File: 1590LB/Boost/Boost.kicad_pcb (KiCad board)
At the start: 2 copper layers, 45 x 45 mm, 44 parts, among them J101 Barrel_Jack_Switch, J102 AudioJack2_SwitchT, J103 AudioJack2_SwitchT, Q101 PMV250, Q201 MMBF5103, Q202 BC847C, Q203 BC857C, Q204 NMB2227A, Q205 DMMT5401, Q206 DMMT5551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

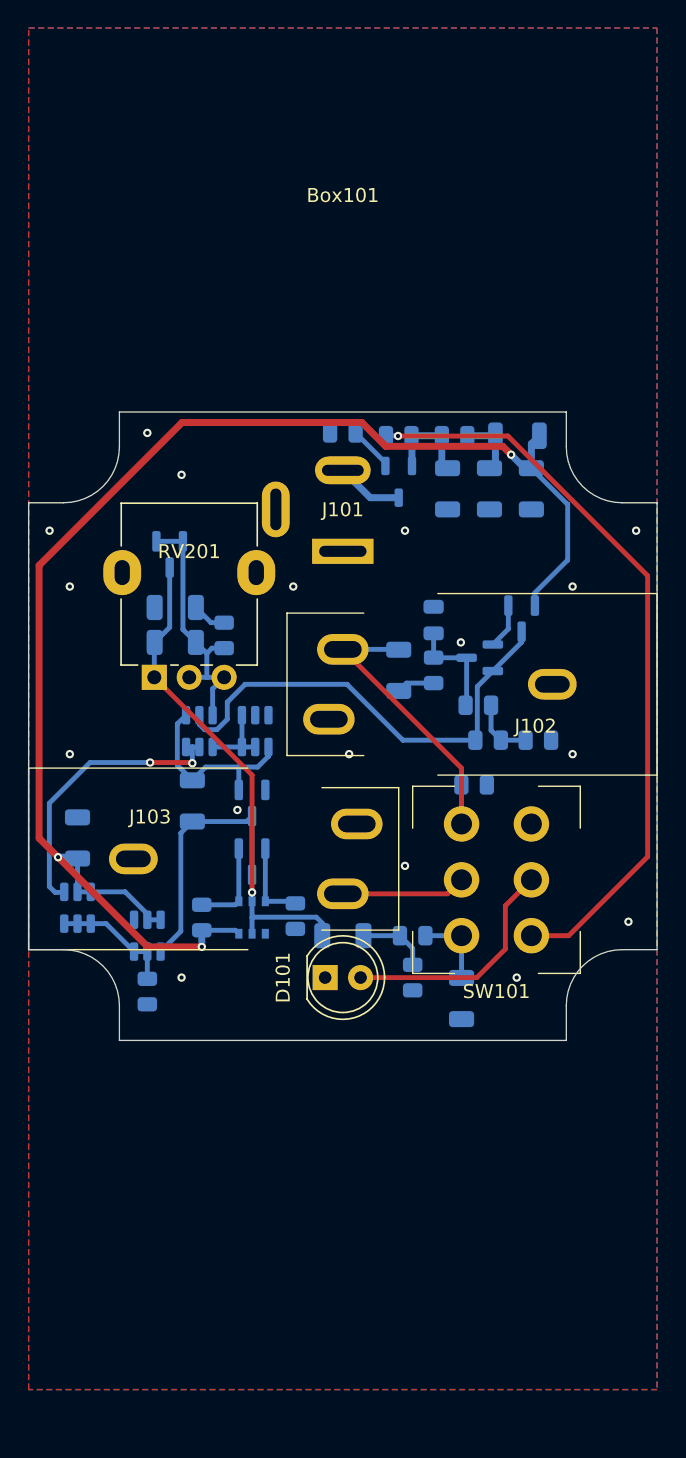
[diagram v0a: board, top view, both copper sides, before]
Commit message: Alternate boost circuit layout
I'm not sure this fits vertically in a 1590LB, but the "everything on
top" model means that the audio jacks are very high up.  Which is not
great from a hole drilling standpoint.

So try putting the audio and DC power jacks on the back of the board,
moving the surface-mount components to the front.

And to make things fit - and because I feel like having done an op-amp
using discrete components - go back to just using an actual op-amp now.

Signed-off-by: Linus Torvalds <torvalds@linux-foundation.org>
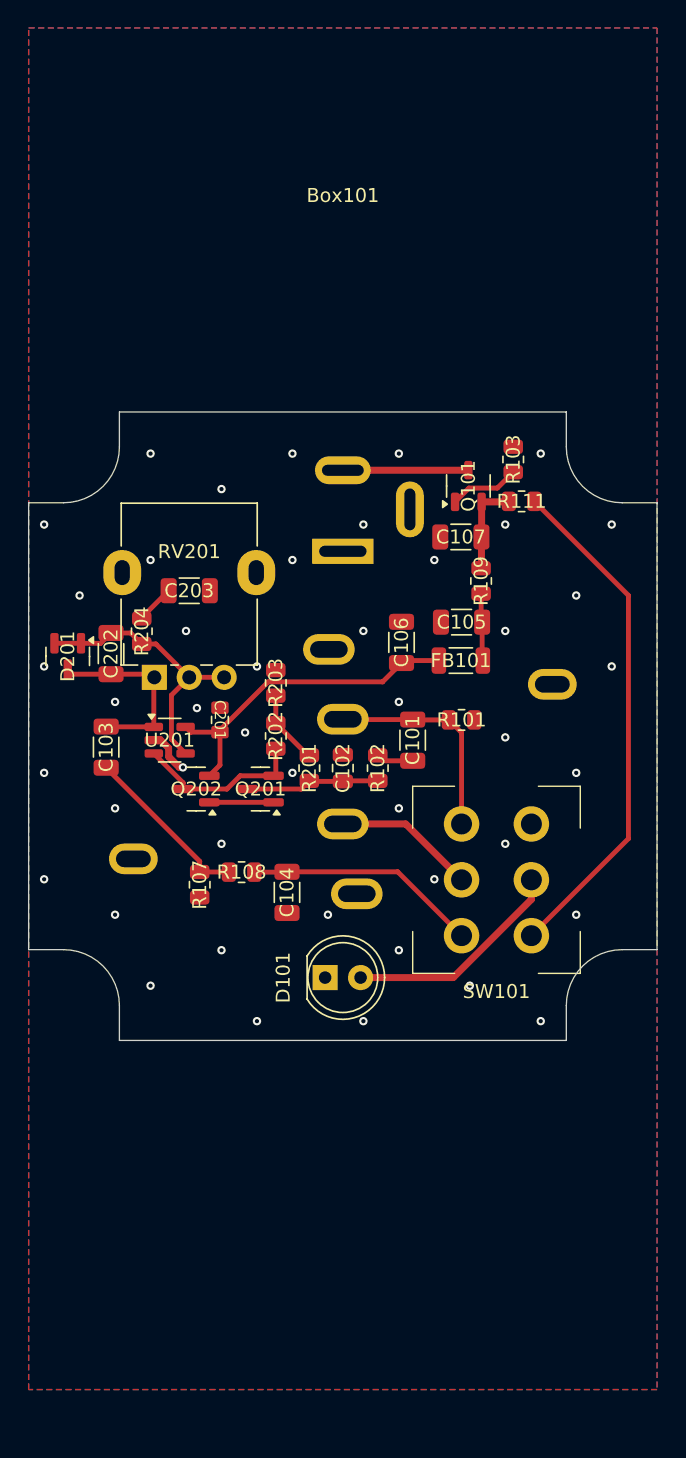
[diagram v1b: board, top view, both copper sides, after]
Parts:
- removed C204: 10uF, Capacitor_SMD:C_1206_3216Metric
- removed the D201 at (93.5, 109.7)
- removed the Q202 at (93.5, 105.5)
- removed Q204: NMB2227A, Package_SO:TSOP-6_1.65x3.05mm_P0.95mm
- removed Q205, Q207, Q208: DMMT5401, Package_TO_SOT_SMD:SOT-23-6
- removed Q206: DMMT5551, Package_TO_SOT_SMD:SOT-23-6
- removed the R204 at (89.9, 113.7)
- removed R205: 47k, Resistor_SMD:R_0805_2012Metric
- removed R207: 5k6, Resistor_SMD:R_0805_2012Metric
- added U201: OPA1655DBV, Package_TO_SOT_SMD:SOT-23-5, F.Cu at (87.6, 101.0)
- C101, C102, C103, C104, C105, C106, C107, C202, C203, FB101, Q101, Q201, R101, R102, R103, R107, R108, R109, R111, R201, R202, R203: moved to F.Cu
- C201: value 1nF -> 0.1uF; footprint Capacitor_SMD:C_1206_3216Metric -> Mylib:C_0704_1810Metric; moved to F.Cu
- D201: renamed from D202; moved to F.Cu
- J101, J102, J103: moved to B.Cu
- Q202: renamed from Q203; moved to F.Cu
- R204: renamed from R206; moved to F.Cu
- moved Q202 26.3 mm to (89.5, 104.5), turned to 180 degrees
- moved C103 21.7 mm to (83.0, 101.5), turned to -90 degrees
- moved R203 19.2 mm to (95.2, 96.9), turned to 90 degrees
- moved Q201 18.3 mm to (94.1, 104.5)
- moved R107 16.6 mm to (89.8, 111.3)
- moved FB101 16.6 mm to (108.5, 95.3), turned to 0 degrees
- moved R202 15.2 mm to (95.2, 100.7), turned to 90 degrees
- moved C104 14.6 mm to (96.0, 111.9)
- moved C106 14.4 mm to (104.2, 94.0), turned to -90 degrees
- moved R108 13.1 mm to (92.8, 110.5)
- moved R201 12.9 mm to (97.6, 103.0), turned to 90 degrees
- moved C102 12.4 mm to (100.0, 103.0)
- moved R103 12.3 mm to (112.2, 80.9), turned to 90 degrees
- moved R109 10.6 mm to (109.9, 89.6), turned to -90 degrees
- moved D201 10.3 mm to (80.3, 95.0)
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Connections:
- C201 pad 1: SRC2 -> GND
- C201 pad 2: LTP_OUT -> +VA
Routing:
- net +VA: track 104.5 -> 23.9 mm, vias 3 -> 0
- net OUTPUT: track 35.7 -> 13.4 mm, vias 1 -> 0
- net BUFFERED: track 33.4 -> 12.3 mm
- net SRC1: track 20.8 -> 0.00 mm, vias 2 -> 0
- net SRC2: track 18.9 -> 0.00 mm
- net Net-(SW101A-C): track 53.7 -> 36.8 mm, vias 1 -> 0
- net LTP_OUT: track 13.9 -> 0.00 mm
- net OUT^{STOMP}: track 5.61 -> 16.7 mm
- net SRC_BASE: track 8.73 -> 0.00 mm
- net Net-(C103-Pad2): track 5.08 -> 12.3 mm
- net Net-(D201-A): track 6.88 -> 0.00 mm
- net Net-(D201-K): track 5.99 -> 0.00 mm
- net IN^{CONN}: track 22.4 -> 16.4 mm
- net Net-(Q205B-C): track 5.32 -> 0.00 mm
- net PWRIN: track 4.81 -> 8.99 mm
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
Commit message: Make the boost circuit a bit more interesting
The clean boost with some clipping was very boring, both from a sound
and a circuit standpoint.

This one isn't any better from a sound standpoint, but at least it's a
bit more interesting.  Instead of a boost pot and clipping diodes, this
has a pot that affects the biasing of the input JFET, and a fixed 10x
voltage boost with a final volume pot.

End result: it also clips, but the clipping is based on how badly the
input transistor is biased, so now you have a bit more control over the
result.

Useful? No.  But I'm back to using discrete components, because the
whole op-amp thing was just too boring.  If I want to use pre-made
circuits, I can do that on the MCU board, let's keep the analog boards
discrete.

That said, I've made the resistors and capacitors small, because I'll
just use this one for the JLCPCB assembly testing.  I did send off a
copy of the MCU board too, which is probably completely stupid - the
first PCBA board I do shouldn't have been that complex.  But maybe it
works (after I figure out the programming - even if the board is fine,
I'll have to do the SW side too to even test it).

Anyway, this one I can have assembled - and test - without then having
to write any code for various i2s things that I have no idea about.

Oh, and I still call this a "1590LB" boost board, even though I actually
ended up deciding that I'll just 3D-print the enclosure.  So it's not
really a 1590LB, it's a 45x50mm board that I'll just print a custom
enclosure for.  I actually really liked how one of my test enclosures
ended up looking, and not being limited to standard aluminum boxes is
liberating.

Signed-off-by: Linus Torvalds <torvalds@linux-foundation.org>
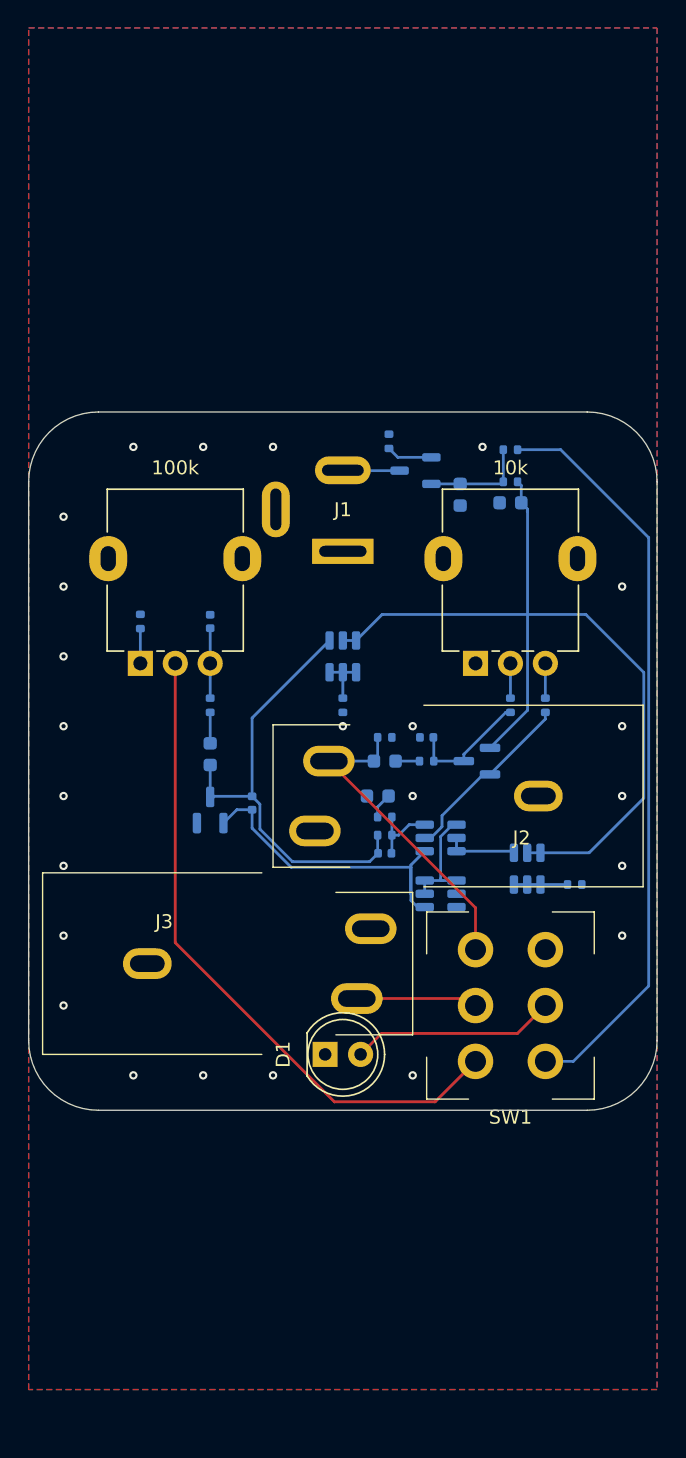
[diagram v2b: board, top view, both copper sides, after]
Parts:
- removed Box101: 1590LB, Mylib:1590LB
- removed C105: 10uF, Capacitor_SMD:C_1206_3216Metric
- removed C106: 1uF, Capacitor_SMD:C_1206_3216Metric
- removed C201: 0.1uF, Mylib:C_0704_1810Metric
- removed D201: MMBD1203, Package_TO_SOT_SMD:SOT-23
- removed FB101: FerriteBead, Inductor_SMD:L_1206_3216Metric
- removed Q201: MMBF5103, Package_TO_SOT_SMD:SOT-23
- removed Q202: BC857C, Package_TO_SOT_SMD:SOT-23
- removed R107: 1MEG, Resistor_SMD:R_0805_2012Metric
- removed R109: 100R, Resistor_SMD:R_0805_2012Metric
- removed R202: 2k2, Resistor_SMD:R_0805_2012Metric
- removed RV201: 100k, Mylib:Potentiometer_9mm_MP
- removed U201: OPA1655DBV, Package_TO_SOT_SMD:SOT-23-5
- added C4: 10uF, Capacitor_SMD:C_0603_1608Metric, B.Cu at (112.0, 84.0)
- added C7: 1nF, Capacitor_SMD:C_0402_1005Metric, B.Cu at (93.5, 105.5)
- added Q2: MMBFJ309L, Package_TO_SOT_SMD:SOT-23, B.Cu at (109.6, 102.5)
- added Q3: BC847C, Package_TO_SOT_SMD:SOT-23, B.Cu at (90.5, 106.0)
- added Q4: DMMT5401, Package_TO_SOT_SMD:SOT-23-6, B.Cu at (107.0, 108.0)
- added Q5: DMMT5551, Package_TO_SOT_SMD:SOT-23-6, B.Cu at (107.0, 112.0)
- added Q6: DMMT5401, Package_TO_SOT_SMD:SOT-23-6, B.Cu at (113.2, 110.2)
- added Q7: DMMT5401, Package_TO_SOT_SMD:SOT-23-6, B.Cu at (100.0, 95.0)
- added R10: 100k, Resistor_SMD:R_0402_1005Metric, B.Cu at (103.0, 107.8)
- added R12: 5k6, Resistor_SMD:R_0402_1005Metric, B.Cu at (116.6, 111.3)
- added R13: 5k6, Resistor_SMD:R_0402_1005Metric, B.Cu at (100.0, 98.5)
- added R5: 33R, Resistor_SMD:R_0402_1005Metric, B.Cu at (112.0, 82.5)
- added R7: 10k, Resistor_SMD:R_0402_1005Metric, B.Cu at (85.5, 92.5)
- added RV1: 100k, Mylib:Potentiometer_9mm_MP, F.Cu at (88.0, 88.0)
- added RV2: 10k, Mylib:Potentiometer_9mm_MP, F.Cu at (112.0, 88.0)
- C1: renamed from C101; footprint Capacitor_SMD:C_1206_3216Metric -> Capacitor_SMD:C_0603_1608Metric; moved to B.Cu
- C2: renamed from C102; footprint Capacitor_SMD:C_0805_2012Metric -> Capacitor_SMD:C_0402_1005Metric; moved to B.Cu
- C3: renamed from C107; footprint Capacitor_SMD:C_1206_3216Metric -> Capacitor_SMD:C_0603_1608Metric; moved to B.Cu
- C5: renamed from C103; value 4.7uF -> 1uF; footprint Capacitor_SMD:C_1206_3216Metric -> Capacitor_SMD:C_0603_1608Metric; moved to B.Cu
- C6: renamed from C104; footprint Capacitor_SMD:C_1206_3216Metric -> Capacitor_SMD:C_0402_1005Metric; moved to B.Cu
- C8: renamed from C202; footprint Capacitor_SMD:C_1206_3216Metric -> Capacitor_SMD:C_0402_1005Metric; moved to B.Cu
- C9: renamed from C203; value 4.7u -> 10uF; footprint Capacitor_SMD:C_1206_3216Metric -> Capacitor_SMD:C_0603_1608Metric; moved to B.Cu
- J1: renamed from J101; moved to F.Cu
- J2: renamed from J102; moved to F.Cu
- J3: renamed from J103; moved to F.Cu
- Q1: renamed from Q101; moved to B.Cu
- R1: renamed from R111; footprint Resistor_SMD:R_0805_2012Metric -> Resistor_SMD:R_0402_1005Metric; moved to B.Cu
- R11: renamed from R204; footprint Resistor_SMD:R_0805_2012Metric -> Resistor_SMD:R_0402_1005Metric; moved to B.Cu
- R2: renamed from R101; footprint Resistor_SMD:R_0805_2012Metric -> Resistor_SMD:R_0402_1005Metric; moved to B.Cu
- R3: renamed from R102; footprint Resistor_SMD:R_0805_2012Metric -> Resistor_SMD:R_0402_1005Metric; moved to B.Cu
- R4: renamed from R103; footprint Resistor_SMD:R_0805_2012Metric -> Resistor_SMD:R_0402_1005Metric; moved to B.Cu
- R6: renamed from R108; footprint Resistor_SMD:R_0805_2012Metric -> Resistor_SMD:R_0402_1005Metric; moved to B.Cu
- R8: renamed from R201; footprint Resistor_SMD:R_0805_2012Metric -> Resistor_SMD:R_0402_1005Metric; moved to B.Cu
- R9: renamed from R203; footprint Resistor_SMD:R_0805_2012Metric -> Resistor_SMD:R_0402_1005Metric; moved to B.Cu
- moved C8 24.3 mm to (103.0, 109.1), turned to 180 degrees
- moved R11 21.9 mm to (103.0, 106.5), turned to 180 degrees
- moved C6 20.2 mm to (90.5, 92.5), turned to -90 degrees
- moved C9 20.0 mm to (102.5, 105.0), turned to 0 degrees
- moved R9 19.4 mm to (114.5, 98.5)
- moved R8 15.1 mm to (112.0, 98.5)
- moved R6 12.2 mm to (90.5, 98.5), turned to 90 degrees
- moved SW1 9.06 mm to (112.0, 120.0)
- moved R4 8.99 mm to (103.3, 79.6)
- moved J2 8.06 mm to (114.0, 105.0)
- moved J3 7.57 mm to (86.0, 117.0)
- moved C5 7.47 mm to (90.5, 102.0), turned to 90 degrees
- moved C2 6.39 mm to (106.0, 100.8), turned to 180 degrees
- moved R2 5.64 mm to (103.0, 100.8)
- moved D1 5.50 mm to (98.7, 123.5)
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- renumbered D101 to D1, SW101 to SW1
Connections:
- C6 pad 2: OUT^{STOMP} -> Net-(C6-Pad2)
- R6 pad 2: OUT^{STOMP} -> Net-(C6-Pad2)
- R8 pad 2: Net-(R201-Pad2) -> Net-(R8-Pad2)
- R9 pad 1: Net-(R201-Pad2) -> BUFFERED
- R9 pad 2: GND -> Net-(R9-Pad2)
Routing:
- net +VA: track 23.9 -> 63.5 mm
- net OUT^{STOMP}: track 16.7 -> 47.4 mm
- net LTP_OUT: track 0.00 -> 23.3 mm
- net OUTPUT: track 13.4 -> 32.3 mm
- net Net-(SW1A-C): track 36.8 -> 53.7 mm
- net FEEDBACK: track 20.2 -> 5.31 mm
- net Net-(C5-Pad2): track 12.3 -> 2.21 mm
- net Net-(Q4B-C): track 0.00 -> 7.91 mm
- net IN^{CONN}: track 16.4 -> 22.9 mm
- net Net-(R201-Pad2): track 5.33 -> 0.00 mm
- net SRC1: track 0.00 -> 5.11 mm
- net Net-(C6-Pad2): track 0.00 -> 5.01 mm
- net PWRIN: track 8.99 -> 4.07 mm
- net Net-(C105-Pad2): track 4.84 -> 0.00 mm
- net Net-(Q201-D): track 4.60 -> 0.00 mm
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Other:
- board size 45 x 45 mm -> 45 x 50 mm

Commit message: 1590LB boost / dirt circuit: add LCSC parts numbers
The PMV250 PNP high-side MOSFET is now a AO3401A, and the BC847C is now
a BC849C instead.  Because those were what I went with at JLCPCB.

It's kind of stupid to have this assembled by machine, since it would be
easy to do by hand (admittedly with slightly different size choices),
and this is not a particularly good design for JLCPCB anyway since all
those matched dual transistors are extended parts etc.

But the point was mainly to do PCBA with a simple board so that I can
actually verify that I did it right.  When the RP2354A comes back, it
will take some coding to get it to do anything at all, so if I screwed
up the hw, it's not going to be as obvious (unless I did it really badly
and the magic smoke escapes).

With this, it's going to be pretty obvious when it doesn't work that my
hw design is just wrong.  Or maybe it works fine - it _should_.  I've
successfully tested a very similar basic circuit, but this does have a
different JFET and some other changes.

Anyway, it's sent off.  When I get back home from travels, I should have
something to test.

Signed-off-by: Linus Torvalds <torvalds@linux-foundation.org>
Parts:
- Q3: value BC847C -> BC849C
- R12, R13: value 5k6 -> 5k1
